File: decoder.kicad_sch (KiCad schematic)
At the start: 5 parts, among them U2 74HC04, U24 74HC08, U3 74HC688, U4 74HC688, U5 74HC4075

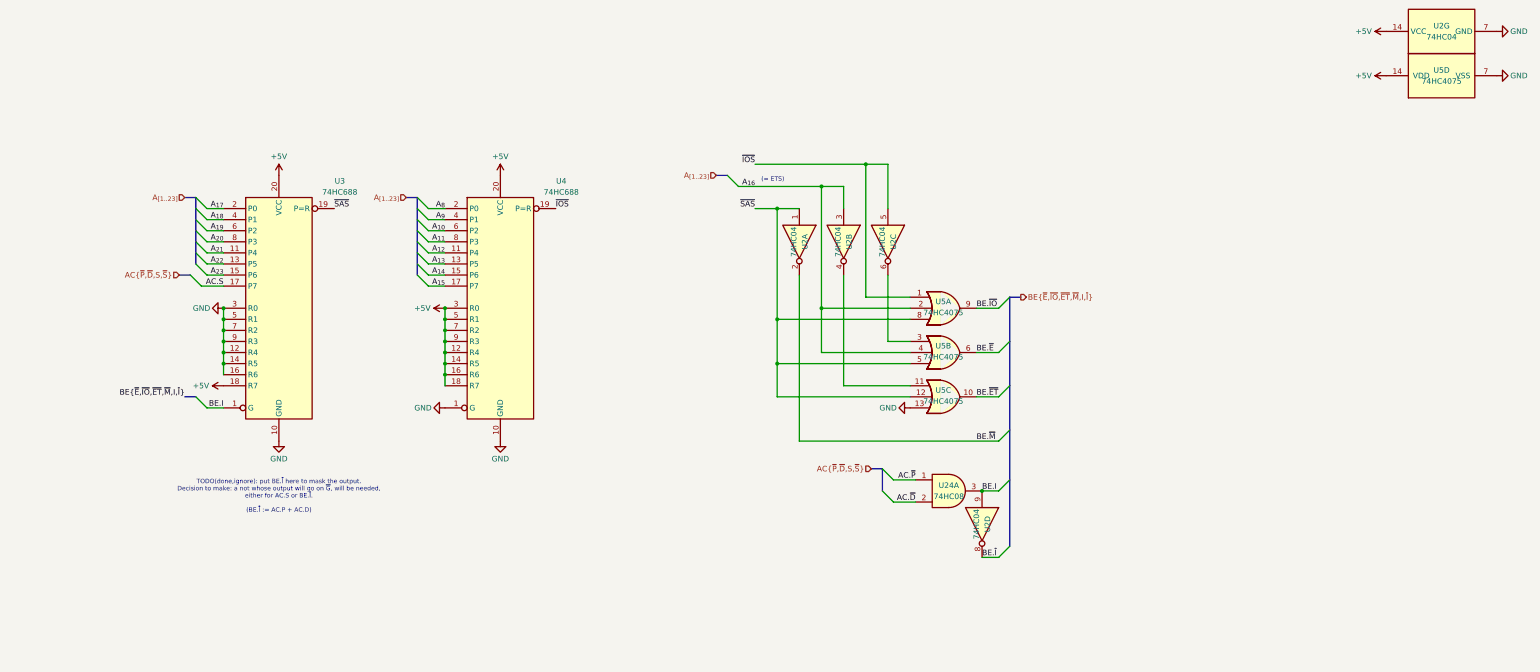
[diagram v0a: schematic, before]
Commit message: finished scheme, footprints not completely assigned yet
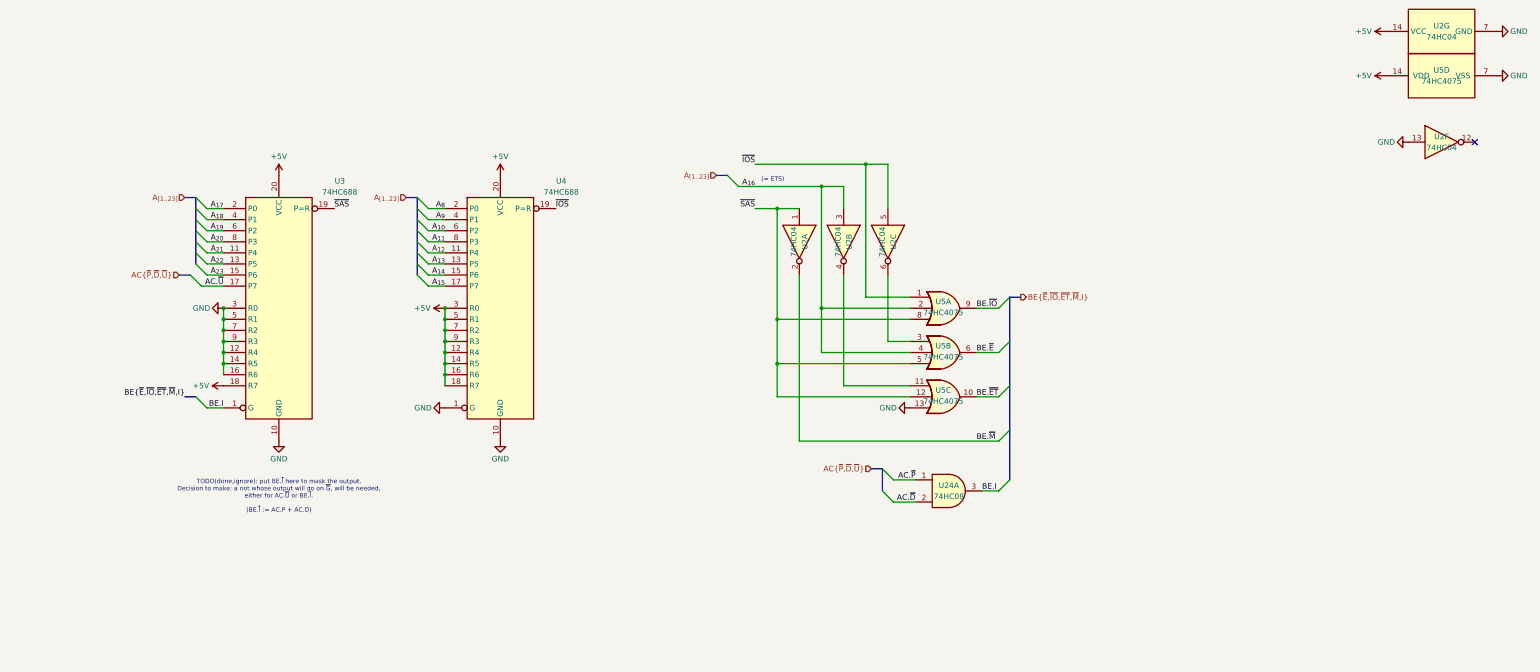
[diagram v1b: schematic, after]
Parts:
- removed unit 4 of U2
- added unit 6 of U2
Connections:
- net GND: now also U2.13
- net AC.S renamed AC.~{U}
- no-connect marks 0 -> 1
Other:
- note added: "TODO(done,ignore): put BE.~{I} here to mask the output. Decision to make: a not whose output will go on ~{G}, will be needed, either for AC.~{U} or BE.~{I}. (BE.~{I} := AC.P + AC.D)"
- note removed: "TODO(done,ignore): put BE.~{I} here to mask the output. Decision to make: a not whose output will go on ~{G}, will be needed, either for AC.S or BE.~{I}. (BE.~{I} := AC.P + AC.D)"

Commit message: done the pcb layout + added the 1M ram bank project
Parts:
- U2, U24, U5: footprint Package_DIP:DIP-14_W7.62mm_Socket -> Package_DIP:DIP-14_W7.62mm
- U3, U4: footprint (none) -> Package_DIP:DIP-20_W7.62mm
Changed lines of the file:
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@@
 			)
 		)
-		(property "Footprint" "Package_DIP:DIP-14_W7.62mm_Socket"
+		(property "Footprint" "Package_DIP:DIP-14_W7.62mm"
 			(at 193.04 48.26 0)
 			(effects
@@
 			)
 		)
-		(property "Footprint" "Package_DIP:DIP-14_W7.62mm_Socket"
+		(property "Footprint" "Package_DIP:DIP-14_W7.62mm"
 			(at 203.2 48.26 0)
 			(effects
@@
 			)
 		)
-		(property "Footprint" ""
+		(property "Footprint" "Package_DIP:DIP-20_W7.62mm"
 			(at 114.3 63.5 0)
 			(effects
@@
 			)
 		)
-		(property "Footprint" "Package_DIP:DIP-14_W7.62mm_Socket"
+		(property "Footprint" "Package_DIP:DIP-14_W7.62mm"
 			(at 330.2 25.4 0)
 			(effects
@@
 			)
 		)
-		(property "Footprint" ""
+		(property "Footprint" "Package_DIP:DIP-20_W7.62mm"
 			(at 63.5 63.5 0)
 			(effects
@@
 			)
 		)
-		(property "Footprint" "Package_DIP:DIP-14_W7.62mm_Socket"
+		(property "Footprint" "Package_DIP:DIP-14_W7.62mm"
 			(at 215.9 73.66 0)
 			(effects
@@
 			)
 		)
-		(property "Footprint" "Package_DIP:DIP-14_W7.62mm_Socket"
+		(property "Footprint" "Package_DIP:DIP-14_W7.62mm"
 			(at 330.2 0 0)
 			(effects
@@
 			)
 		)
-		(property "Footprint" "Package_DIP:DIP-14_W7.62mm_Socket"
+		(property "Footprint" "Package_DIP:DIP-14_W7.62mm"
 			(at 215.9 63.5 0)
 			(effects
@@
 			)
 		)
-		(property "Footprint" "Package_DIP:DIP-14_W7.62mm_Socket"
+		(property "Footprint" "Package_DIP:DIP-14_W7.62mm"
 			(at 215.9 83.82 0)
 			(effects
@@
 			)
 		)
-		(property "Footprint" "Package_DIP:DIP-14_W7.62mm_Socket"
+		(property "Footprint" "Package_DIP:DIP-14_W7.62mm"
 			(at 217.17 105.41 0)
 			(effects
@@
 			)
 		)
-		(property "Footprint" "Package_DIP:DIP-14_W7.62mm_Socket"
+		(property "Footprint" "Package_DIP:DIP-14_W7.62mm"
 			(at 182.88 48.26 0)
 			(effects
@@
 			)
 		)
-		(property "Footprint" "Package_DIP:DIP-14_W7.62mm_Socket"
+		(property "Footprint" "Package_DIP:DIP-14_W7.62mm"
 			(at 330.2 10.16 0)
 			(effects

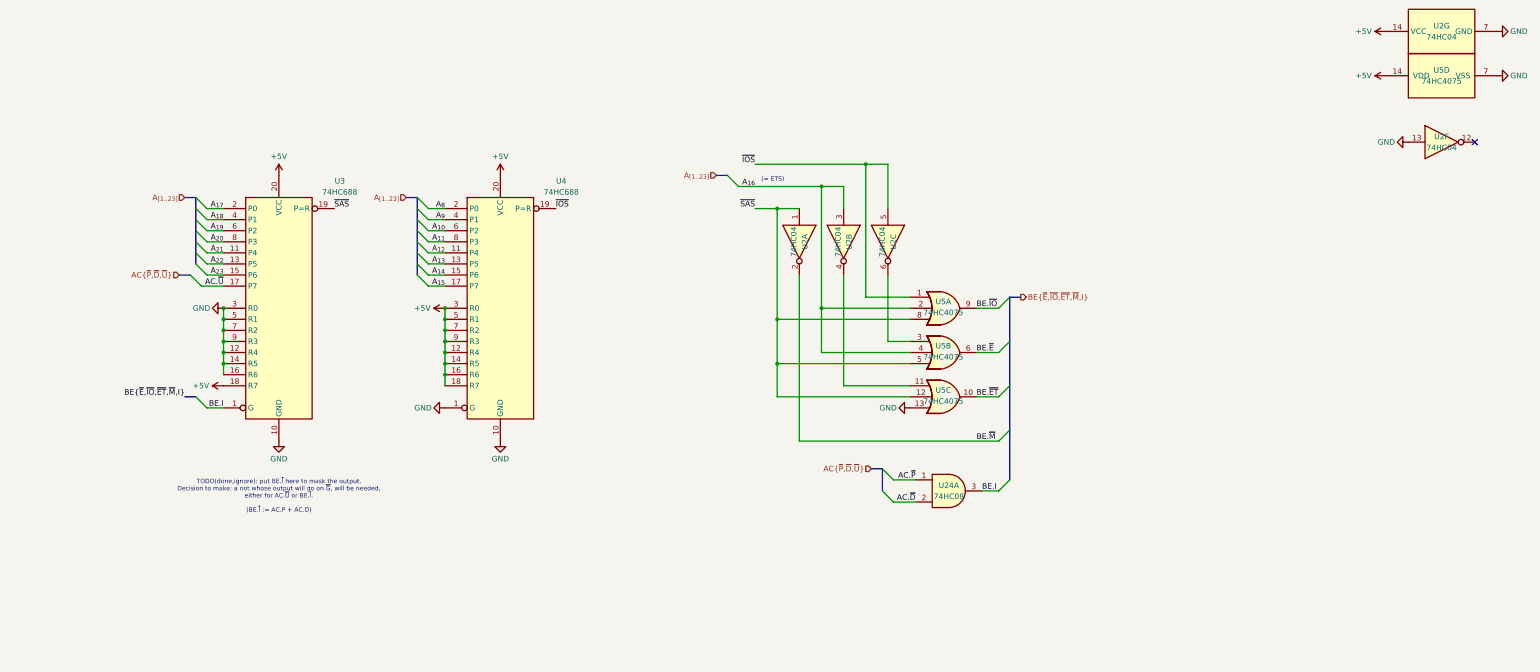
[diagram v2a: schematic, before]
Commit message: first commit: scheme ok [decoder]: 	- new spv. address space [mmu]: 	- removed pidreg 	- switched back to 8Kb mmu rams [ram/peripherals]: 	- added ground pins to connectors [misc]: 	- added DMA support 	- added clock halfer
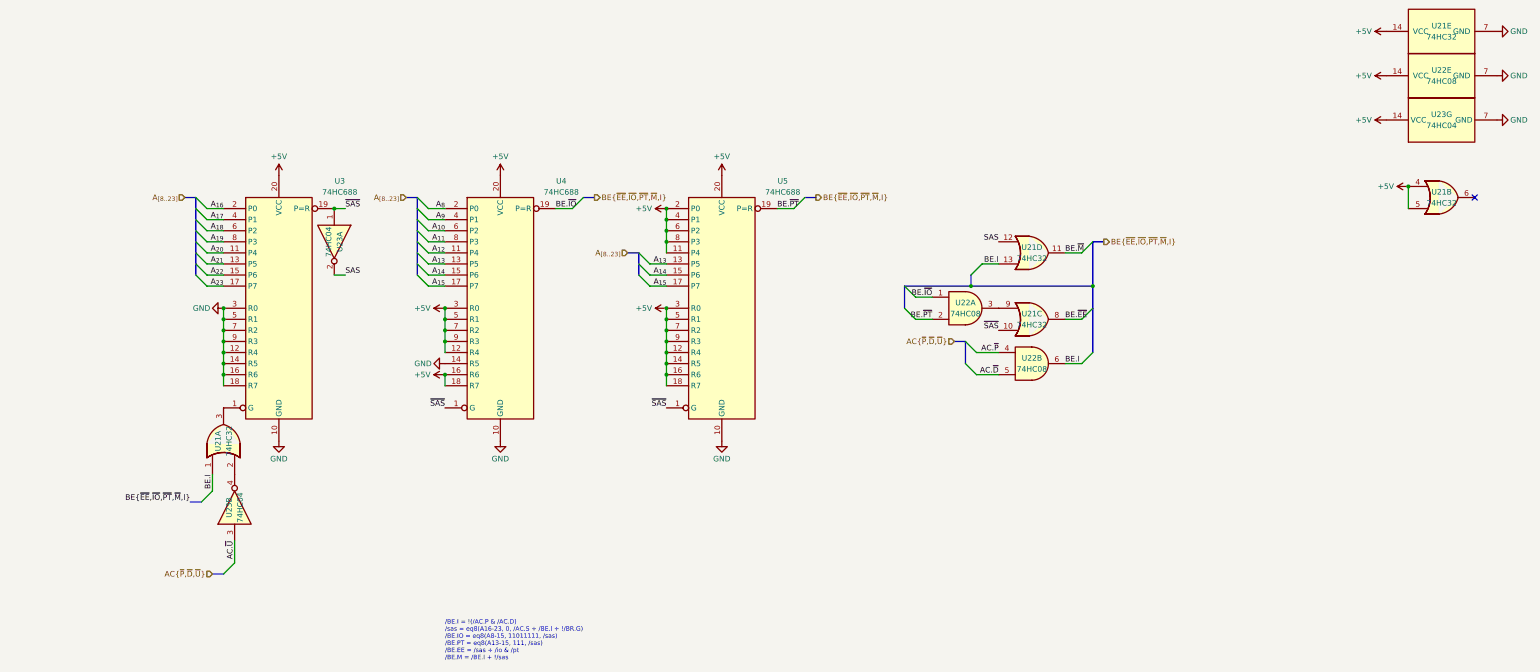
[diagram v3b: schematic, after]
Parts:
- removed U2: 74HC04, Package_DIP:DIP-14_W7.62mm, symbol 74xx:74LS04
- removed U24: 74HC08, Package_DIP:DIP-14_W7.62mm, symbol 74xx:74LS08
- removed U5: 74HC4075, Package_DIP:DIP-14_W7.62mm, symbol 4xxx:4075
- added U21: 74HC32, symbol 74xx:74LS32
- added U22: 74HC08, symbol 74xx:74LS08
- added U23: 74HC04, symbol 74xx:74LS04
- added U5: 74HC688, Package_DIP:DIP-20_W7.62mm, symbol 74xx:74HC688
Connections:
- net ~{IOS} is gone; now on net BE.~{IO}: U4.19 (P=R)
- net +5V: now also U21.14 (VCC), U21.4, U21.5, U22.14 (VCC), U23.14 (VCC), U5.11 (P4), U5.12 (R4), U5.14 (R5), U5.16 (R6), U5.18 (R7), U5.2 (P0), U5.20 (VCC), U5.3 (R0), U5.4 (P1), U5.5 (R1), U5.6 (P2), U5.7 (R2), U5.8 (P3), U5.9 (R3); no longer U3.18 (R7), U4.14 (R5)
- net AC.~{D}: now also U22.5
- net AC.~{P}: now also U22.4
- net AC.~{U}: now also U23.3; no longer U3.17 (P7)
- net A_{13}: now also U5.13 (P5)
- net A_{14}: now also U5.15 (P6)
- net A_{15}: now also U5.17 (P7)
- net A_{16}: now also U3.2 (P0)
- net A_{17}: now also U3.4 (P1); no longer U3.2 (P0)
- net A_{18}: now also U3.6 (P2); no longer U3.4 (P1)
- net A_{19}: now also U3.8 (P3); no longer U3.6 (P2)
- net A_{20}: now also U3.11 (P4); no longer U3.8 (P3)
- net A_{21}: now also U3.13 (P5); no longer U3.11 (P4)
- net A_{22}: now also U3.15 (P6); no longer U3.13 (P5)
- net A_{23}: now also U3.17 (P7); no longer U3.15 (P6)
- net BE.I: now also U21.1, U21.13, U22.6; no longer U3.1 (G)
- net BE.~{IO}: now also U22.1
- net BE.~{M}: now also U21.11
- net GND: now also U3.18 (R7), U4.14 (R5), U21.7 (GND), U22.7 (GND), U23.7 (GND), U5.10 (GND); no longer U4.1 (G)
- net ~{SAS}: now also U4.1 (G), U21.10, U23.1, U5.1 (G)
- new net: U21.9, U22.3
- new net: U21.3, U3.1 (G)
- new net: U21.2, U23.4
- new net BE.~{EE}: U21.8
- new net BE.~{PT}: U22.2, U5.19 (P=R)
- new net SAS: U21.12, U23.2
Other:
- note added: "/BE.I = !(/AC.P & /AC.D) /sas = eq8(A16-23, 0, /AC.S + /BE.I + !/BR.G) /BE.IO = eq8(A8-15, 11011111, /sas) /BE.PT = eq8(A13-15, 111, /sas) /BE.EE = /sas + /io & /pt /BE.M = /BE.I + !/sas"
- note removed: "(= ETS)"
- note removed: "TODO(done,ignore): put BE.~{I} here to mask the output. Decision to make: a not whose output will go on ~{G}, will be needed, either for AC.~{U} or BE.~{I}. (BE.~{I} := AC.P + AC.D)"

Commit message: assigned footprints
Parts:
- U21, U22, U23: footprint (none) -> Package_DIP:DIP-14_W7.62mm
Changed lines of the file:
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@@
 			)
 		)
-		(property "Footprint" ""
+		(property "Footprint" "Package_DIP:DIP-14_W7.62mm"
 			(at 220.98 63.5 0)
 			(effects
@@
 			)
 		)
-		(property "Footprint" ""
+		(property "Footprint" "Package_DIP:DIP-14_W7.62mm"
 			(at 330.2 10.16 0)
 			(effects
@@
 			)
 		)
-		(property "Footprint" ""
+		(property "Footprint" "Package_DIP:DIP-14_W7.62mm"
 			(at 236.22 66.04 0)
 			(effects
@@
 			)
 		)
-		(property "Footprint" ""
+		(property "Footprint" "Package_DIP:DIP-14_W7.62mm"
 			(at 236.22 76.2 0)
 			(effects
@@
 			)
 		)
-		(property "Footprint" ""
+		(property "Footprint" "Package_DIP:DIP-14_W7.62mm"
 			(at 330.2 0 0)
 			(effects
@@
 			)
 		)
-		(property "Footprint" ""
+		(property "Footprint" "Package_DIP:DIP-14_W7.62mm"
 			(at 53.34 109.22 0)
 			(effects
@@
 			)
 		)
-		(property "Footprint" ""
+		(property "Footprint" "Package_DIP:DIP-14_W7.62mm"
 			(at 330.2 38.1 0)
 			(effects
@@
 			)
 		)
-		(property "Footprint" ""
+		(property "Footprint" "Package_DIP:DIP-14_W7.62mm"
 			(at 50.8 93.98 0)
 			(effects
@@
 			)
 		)
-		(property "Footprint" ""
+		(property "Footprint" "Package_DIP:DIP-14_W7.62mm"
 			(at 76.2 48.26 0)
 			(effects
@@
 			)
 		)
-		(property "Footprint" ""
+		(property "Footprint" "Package_DIP:DIP-14_W7.62mm"
 			(at 236.22 50.8 0)
 			(effects
@@
 			)
 		)
-		(property "Footprint" ""
+		(property "Footprint" "Package_DIP:DIP-14_W7.62mm"
 			(at 330.2 20.32 0)
 			(effects

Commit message: applied sf68 & ps2 fixes stash from master
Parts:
- added U17: 74HC04, Package_DIP:DIP-14_W7.62mm, symbol 74xx:74LS04
- renumbered U21 to U23, U22 to U28
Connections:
- net at U28.3: now also U17.11; no longer U23.9
- new net: U17.10, U23.9
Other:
- moved on the sheet: U23C, U23D, U28A, U28B

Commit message: 1.0.0 commit
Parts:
- removed unit 2 of U21
- removed unit 2 of U23
- added unit 2 of U17
- added unit 2 of U23
- added unit 3 of U28
- renumbered U3 to U12, U4 to U15, U23 to U17, U5 to U18, U21 to U23, U22 to U28
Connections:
- net AC.~{U}: now also U17.3
- net BE.I: now also U23.5; no longer U23.1
- net ~{SAS}: now also U28.8; no longer U12.19 (P=R)
- net at U23.2: now also U23.6
- new net: U17.4, U23.1
- new net: U12.19 (P=R), U28.10
- new net DMA.G: U23.4
- new net DMA.~{SAS}: U28.9
- no-connect marks 1 -> 0
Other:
- note removed: "/BE.I = !(/AC.P & /AC.D) /sas = eq8(A16-23, 0, /AC.S + /BE.I + !/BR.G) /BE.IO = eq8(A8-15, 11011111, /sas) /BE.PT = eq8(A13-15, 111, /sas) /BE.EE = /sas + /io & /pt /BE.M = /BE.I + !/sas"
- moved on the sheet: U12, U15, U17A, U17E, U18, U23A, U23C, U23D, U28A, U28B
